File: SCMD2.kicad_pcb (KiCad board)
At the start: 2 copper layers, 86.9 x 68.1 mm, 71 parts, among them IC1 ATMEGA8-P, J1 PWR JACK, J2 ICSP, J3 SKIN_EL, J4 MINIUSB, Q1 2N3904, SW1 SW_GENERIC, SW2 SW_PUSH, U1 OP177, U2 OP177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

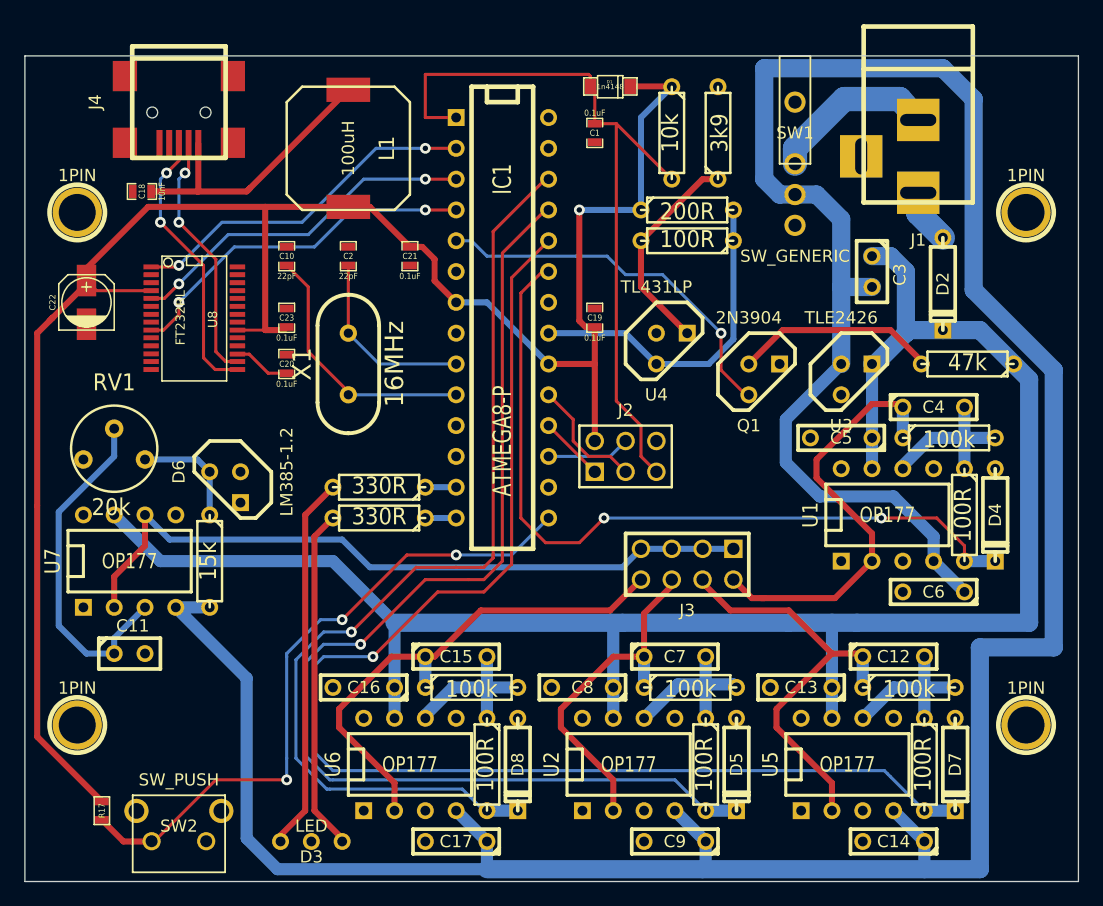
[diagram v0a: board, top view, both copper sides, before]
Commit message: Add filling zone and connect GND.
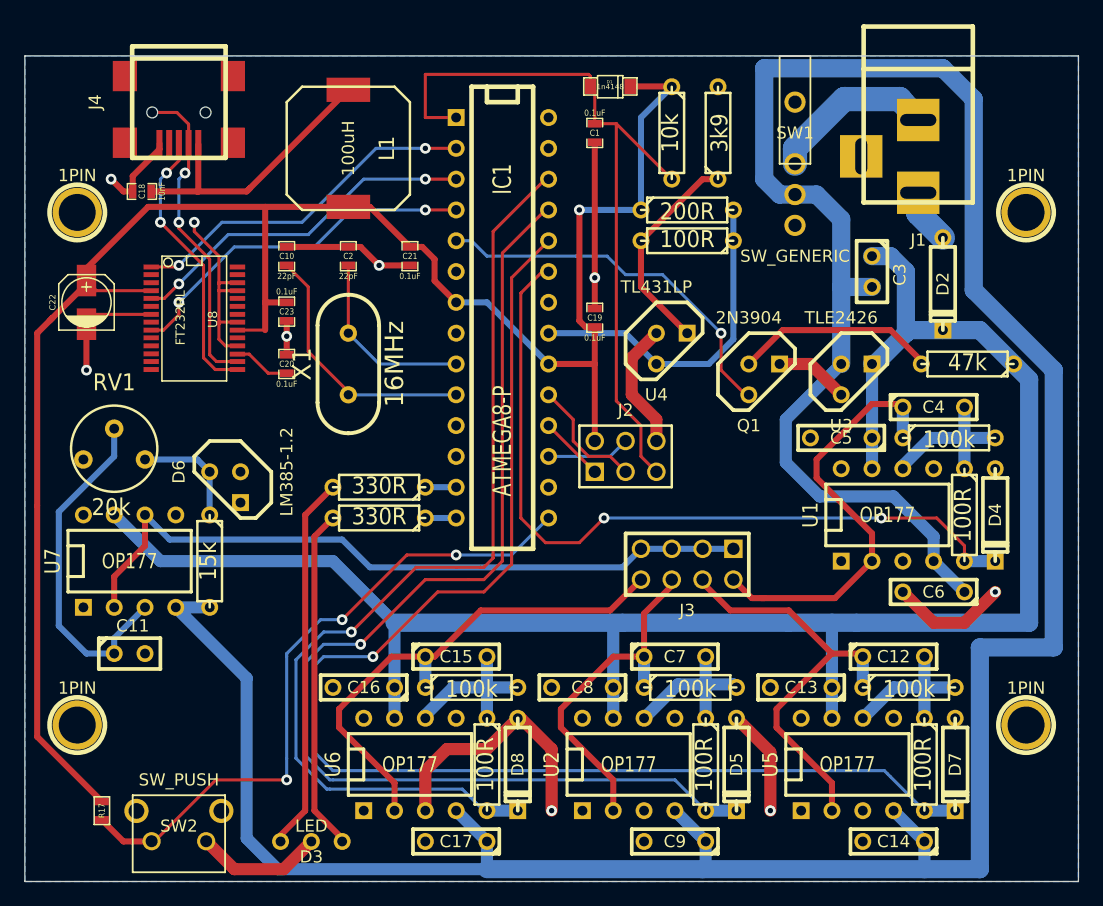
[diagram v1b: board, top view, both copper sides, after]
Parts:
- moved C23 0.51 mm to (49.5, 51.6), turned to 270 degrees
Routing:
- net GND: track 0.00 -> 128.3 mm, vias 0 -> 9
- net N-0000042: track 20.8 -> 26.3 mm
- net +5V: track 159.3 -> 158.5 mm
- added copper zone on B.Cu, net GND

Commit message: Add board info.
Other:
- board text added: "CeDEx Labs, 2014"
- board text added: "SCMD v.0.1"
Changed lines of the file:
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@@
     (area 27.889999 27.614879 114.858001 98.602001)
     (thickness 1.6)
-    (drawings 5)
+    (drawings 7)
     (tracks 477)
     (zones 0)
@@
   )
   (setup
-    (last_trace_width 1)
+    (last_trace_width 0.254)
     (user_trace_width 0.5)
     (user_trace_width 1)
@@
     (visible_elements 7FFFFFFF)
     (pcbplotparams
-      (layerselection 3178497)
+      (layerselection 279609345)
       (usegerberextensions true)
       (excludeedgelayer true)
@@
       (outputformat 1)
       (mirror false)
-      (drillshape 1)
+      (drillshape 0)
       (scaleselection 1)
-      (outputdirectory ""))
+      (outputdirectory gerber/))
   )
   (net 0 "")
@@
     )
   )
+  (gr_text "CeDEx Labs, 2014" (at 66.548 74.676) (layer F.SilkS)
+    (effects (font (size 1.5 1.5) (thickness 0.3)))
+  )
+  (gr_text "SCMD v.0.1" (at 62.738 77.216) (layer F.SilkS)
+    (effects (font (size 1.5 1.5) (thickness 0.3)))
+  )
   (target plus (at 41.91 38.1) (size 0.005) (width 0.1) (layer Edge.Cuts))

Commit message: Fix mini-usb mod and improve ground filling connectivity.
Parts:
- J4: footprint USB_MINI_B -> USB_MINI_B_fixed
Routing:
- net GND: track 128.3 -> 143.9 mm, vias 9 -> 8
- net N-0000042: track 26.3 -> 21.3 mm
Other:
- board text removed: "SCMD v.0.1"
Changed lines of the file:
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@@
 (kicad_pcb (version 3) (host pcbnew "(2013-07-07 BZR 4022)-stable")
   (general
-    (links 155)
+    (links 154)
     (no_connects 0)
     (area 27.889999 27.614879 114.858001 98.602001)
     (thickness 1.6)
-    (drawings 7)
-    (tracks 477)
+    (drawings 6)
+    (tracks 475)
     (zones 0)
     (modules 71)
@@
     (15 F.Cu signal)
     (0 B.Cu signal)
+    (16 B.Adhes user)
     (17 F.Adhes user)
+    (18 B.Paste user)
     (19 F.Paste user)
+    (20 B.SilkS user)
     (21 F.SilkS user)
+    (22 B.Mask user)
     (23 F.Mask user)
     (28 Edge.Cuts user)
   )
   (setup
-    (last_trace_width 0.254)
+    (last_trace_width 1)
     (user_trace_width 0.5)
     (user_trace_width 1)
@@
     (visible_elements 7FFFFFFF)
     (pcbplotparams
-      (layerselection 279609345)
+      (layerselection 285179905)
       (usegerberextensions true)
       (excludeedgelayer true)
@@
       (drillshape 0)
       (scaleselection 1)
-      (outputdirectory gerber/))
+      (outputdirectory D:/xmega128/SCMD2/design/))
   )
   (net 0 "")
@@
     (add_net VEE)
   )
-  (module USB_MINI_B (layer F.Cu)
-    (at 40.64 34.29 270)
-    (descr "USB Mini-B 5-pin SMD connector")
-    (tags "USB, Mini-B, connector")
-    (fp_text reference J4 (at 0 6.90118 270) (layer F.SilkS)
-      (effects (font (size 1.016 1.016) (thickness 0.2032)))
-    )
-    (fp_text value MINIUSB (at 0 -7.0993 270) (layer F.SilkS) hide
-      (effects (font (size 1.016 1.016) (thickness 0.2032)))
-    )
-    (fp_line (start -3.59918 -3.85064) (end -3.59918 3.85064) (layer F.SilkS) (width 0.381))
-    (fp_line (start -4.59994 -3.85064) (end -4.59994 3.85064) (layer F.SilkS) (width 0.381))
-    (fp_line (start -4.59994 3.85064) (end 4.59994 3.85064) (layer F.SilkS) (width 0.381))
-    (fp_line (start 4.59994 3.85064) (end 4.59994 -3.85064) (layer F.SilkS) (width 0.381))
-    (fp_line (start 4.59994 -3.85064) (end -4.59994 -3.85064) (layer F.SilkS) (width 0.381))
-    (pad 1 smd rect (at 3.44932 -1.6002 270) (size 2.30124 0.50038)
-      (layers F.Cu F.Paste F.Mask)
-      (net 29 N-0000041)
-    )
-    (pad 2 smd rect (at 3.44932 -0.8001 270) (size 2.30124 0.50038)
-      (layers F.Cu F.Paste F.Mask)
-      (net 30 N-0000042)
-    )
-    (pad 3 smd rect (at 3.44932 0 270) (size 2.30124 0.50038)
-      (layers F.Cu F.Paste F.Mask)
-      (net 31 N-0000043)
-    )
-    (pad 4 smd rect (at 3.44932 0.8001 270) (size 2.30124 0.50038)
-      (layers F.Cu F.Paste F.Mask)
-    )
-    (pad 5 smd rect (at 3.44932 1.6002 270) (size 2.30124 0.50038)
-      (layers F.Cu F.Paste F.Mask)
-      (net 23 GND)
-    )
-    (pad 6 smd rect (at 3.35026 -4.45008 270) (size 2.49936 1.99898)
-      (layers F.Cu F.Paste F.Mask)
-    )
-    (pad 7 smd rect (at -2.14884 -4.45008 270) (size 2.49936 1.99898)
-      (layers F.Cu F.Paste F.Mask)
-    )
-    (pad 8 smd rect (at 3.35026 4.45008 270) (size 2.49936 1.99898)
-      (layers F.Cu F.Paste F.Mask)
-    )
-    (pad 9 smd rect (at -2.14884 4.45008 270) (size 2.49936 1.99898)
-      (layers F.Cu F.Paste F.Mask)
-    )
-    (pad "" np_thru_hole circle (at 0.8509 -2.19964 270) (size 0.89916 0.89916) (drill 0.89916)
-      (layers *.Cu *.Mask F.SilkS)
-    )
-    (pad 2 np_thru_hole circle (at 0.8509 2.19964 270) (size 0.89916 0.89916) (drill 0.89916)
-      (layers *.Cu *.Mask F.SilkS)
-      (net 30 N-0000042)
-    )
-  )
   (module TO92 (layer F.Cu)
     (at 81.28 54.61)
@@
     )
   )
-  (gr_text "CeDEx Labs, 2014" (at 66.548 74.676) (layer F.SilkS)
-    (effects (font (size 1.5 1.5) (thickness 0.3)))
+  (module USB_MINI_B_fixed (layer F.Cu)
+    (at 40.64 34.29 270)
+    (descr "USB Mini-B 5-pin SMD connector")
+    (tags "USB, Mini-B, connector")
+    (fp_text reference J4 (at 0 6.90118 270) (layer F.SilkS)
+      (effects (font (size 1.016 1.016) (thickness 0.2032)))
+    )
+    (fp_text value MINIUSB (at 0 -7.0993 270) (layer F.SilkS) hide
+      (effects (font (size 1.016 1.016) (thickness 0.2032)))
+    )
+    (fp_line (start -3.59918 -3.85064) (end -3.59918 3.85064) (layer F.SilkS) (width 0.381))
+    (fp_line (start -4.59994 -3.85064) (end -4.59994 3.85064) (layer F.SilkS) (width 0.381))
+    (fp_line (start -4.59994 3.85064) (end 4.59994 3.85064) (layer F.SilkS) (width 0.381))
+    (fp_line (start 4.59994 3.85064) (end 4.59994 -3.85064) (layer F.SilkS) (width 0.381))
+    (fp_line (start 4.59994 -3.85064) (end -4.59994 -3.85064) (layer F.SilkS) (width 0.381))
+    (pad 1 smd rect (at 3.44932 -1.6002 270) (size 2.30124 0.50038)
+      (layers F.Cu F.Paste F.Mask)
+      (net 29 N-0000041)
+    )
+    (pad 2 smd rect (at 3.44932 -0.8001 270) (size 2.30124 0.50038)
+      (layers F.Cu F.Paste F.Mask)
+      (net 30 N-0000042)
+    )
+    (pad 3 smd rect (at 3.44932 0 270) (size 2.30124 0.50038)
+      (layers F.Cu F.Paste F.Mask)
+      (net 31 N-0000043)
+    )
+    (pad 4 smd rect (at 3.44932 0.8001 270) (size 2.30124 0.50038)
+      (layers F.Cu F.Paste F.Mask)
+    )
+    (pad 5 smd rect (at 3.44932 1.6002 270) (size 2.30124 0.50038)
+      (layers F.Cu F.Paste F.Mask)
+      (net 23 GND)
+    )
+    (pad 6 smd rect (at 3.35026 -4.45008 270) (size 2.49936 1.99898)
+      (layers F.Cu F.Paste F.Mask)
+    )
+    (pad 7 smd rect (at -2.14884 -4.45008 270) (size 2.49936 1.99898)
+      (layers F.Cu F.Paste F.Mask)
+    )
+    (pad 8 smd rect (at 3.35026 4.45008 270) (size 2.49936 1.99898)
+      (layers F.Cu F.Paste F.Mask)
+    )
+    (pad 9 smd rect (at -2.14884 4.45008 270) (size 2.49936 1.99898)
+      (layers F.Cu F.Paste F.Mask)
+    )
+    (pad "" np_thru_hole circle (at 0.8509 -2.19964 270) (size 0.89916 0.89916) (drill 0.89916)
+      (layers *.Cu *.Mask F.SilkS)
+    )
+    (pad "" np_thru_hole circle (at 0.8509 2.19964 270) (size 0.89916 0.89916) (drill 0.89916)
+      (layers *.Cu *.Mask F.SilkS)
+    )
   )
-  (gr_text "SCMD v.0.1" (at 62.738 77.216) (layer F.SilkS)
+  (gr_text "CeDEx Labs, 2014" (at 66.548 74.676) (layer F.SilkS)
     (effects (font (size 1.5 1.5) (thickness 0.3)))
   )
@@
   (segment (start 51.308 54.864) (end 51.308 49.53) (width 0.254) (layer F.Cu) (net 22))
   (segment (start 54.61 58.166) (end 51.308 54.864) (width 0.254) (layer F.Cu) (net 22))
+  (segment (start 100.33 74.676) (end 102.87 77.216) (width 1) (layer F.Cu) (net 23) (status 400000))
+  (segment (start 110.744 67.31) (end 107.95 64.516) (width 1) (layer F.Cu) (net 23) (status 800000))
+  (segment (start 110.744 67.564) (end 110.744 67.31) (width 1) (layer F.Cu) (net 23))
+  (segment (start 110.744 77.216) (end 110.744 67.564) (width 1) (layer F.Cu) (net 23))
+  (segment (start 102.87 77.216) (end 110.744 77.216) (width 1) (layer F.Cu) (net 23))
   (segment (start 80.01 62.23) (end 80.01 60.452) (width 1) (layer F.Cu) (net 23))
   (segment (start 77.978 55.372) (end 80.01 53.34) (width 1) (layer F.Cu) (net 23))
   (segment (start 77.978 58.42) (end 77.978 55.372) (width 1) (layer F.Cu) (net 23))
   (segment (start 80.01 60.452) (end 77.978 58.42) (width 1) (layer F.Cu) (net 23))
-  (segment (start 100.33 74.676) (end 102.87 77.216) (width 1) (layer F.Cu) (net 23))
-  (via (at 107.95 74.676) (size 0.889) (layers F.Cu B.Cu) (net 23))
-  (segment (start 105.41 77.216) (end 107.95 74.676) (width 1) (layer F.Cu) (net 23))
-  (segment (start 102.87 77.216) (end 105.41 77.216) (width 1) (layer F.Cu) (net 23))
   (segment (start 60.96 92.71) (end 60.96 89.408) (width 1) (layer F.Cu) (net 23))
   (segment (start 66.04 87.63) (end 68.58 85.09) (width 1) (layer F.Cu) (net 23))
@@
   (segment (start 46.482 41.402) (end 54.61 33.274) (width 0.5) (layer F.Cu) (net 29))
   (segment (start 42.164 37.81552) (end 42.2402 37.73932) (width 0.254) (layer F.Cu) (net 29))
-  (segment (start 38.44036 35.1409) (end 40.4749 35.1409) (width 0.254) (layer F.Cu) (net 30))
-  (segment (start 41.4401 36.1061) (end 41.4401 37.73932) (width 0.254) (layer F.Cu) (net 30))
-  (segment (start 40.4749 35.1409) (end 41.4401 36.1061) (width 0.254) (layer F.Cu) (net 30))
   (segment (start 40.64 44.196) (end 40.64 44.704) (width 0.254) (layer F.Cu) (net 30))
   (via (at 40.64 44.196) (size 0.889) (layers F.Cu B.Cu) (net 30))

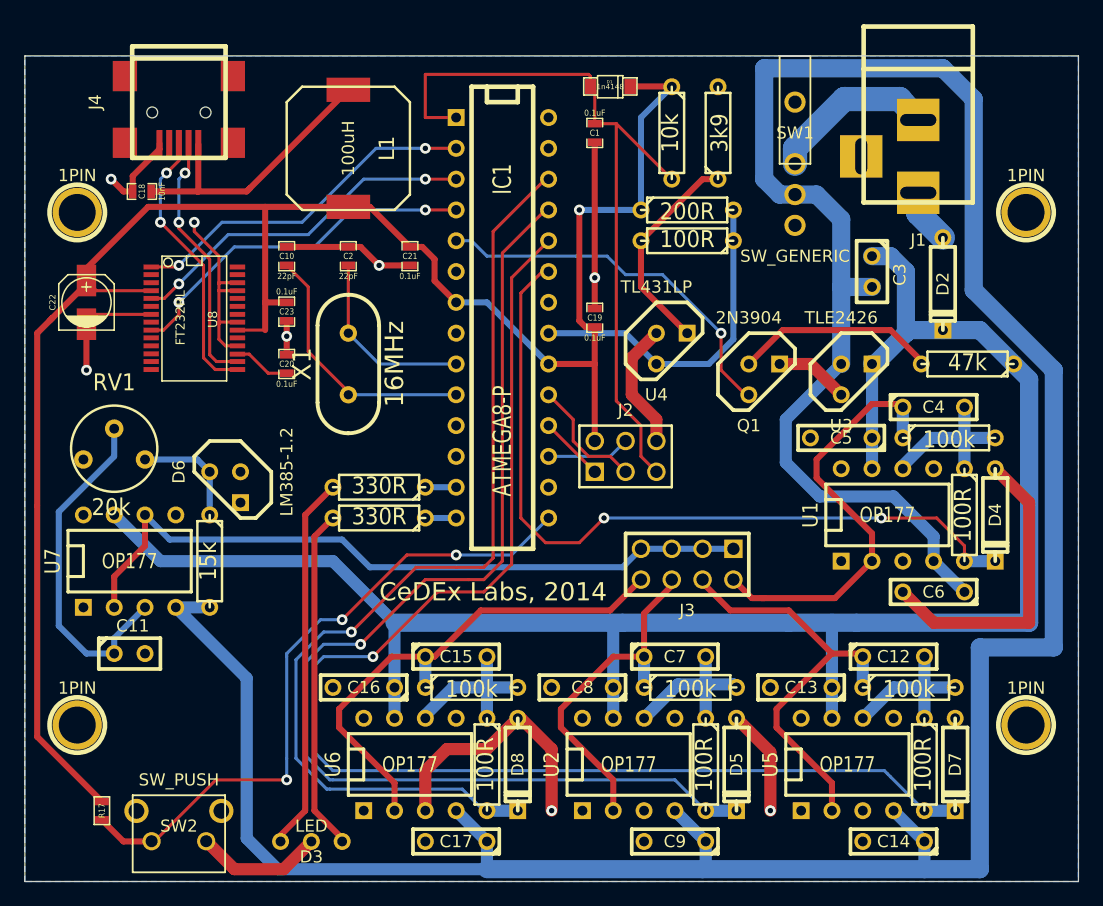
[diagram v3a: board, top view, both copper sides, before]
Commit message: Refactor PCB and release SCMD2 V.0.1.2
* Fix L1 footprint,
* Refactor tracks to avoid their accidential damage,
* Replace TO92 footprints to match case type,
* Use SM0603 for R1,
* Add pin labels for J2 and J3,
* Add D3 LED labels,
* Add board version label.
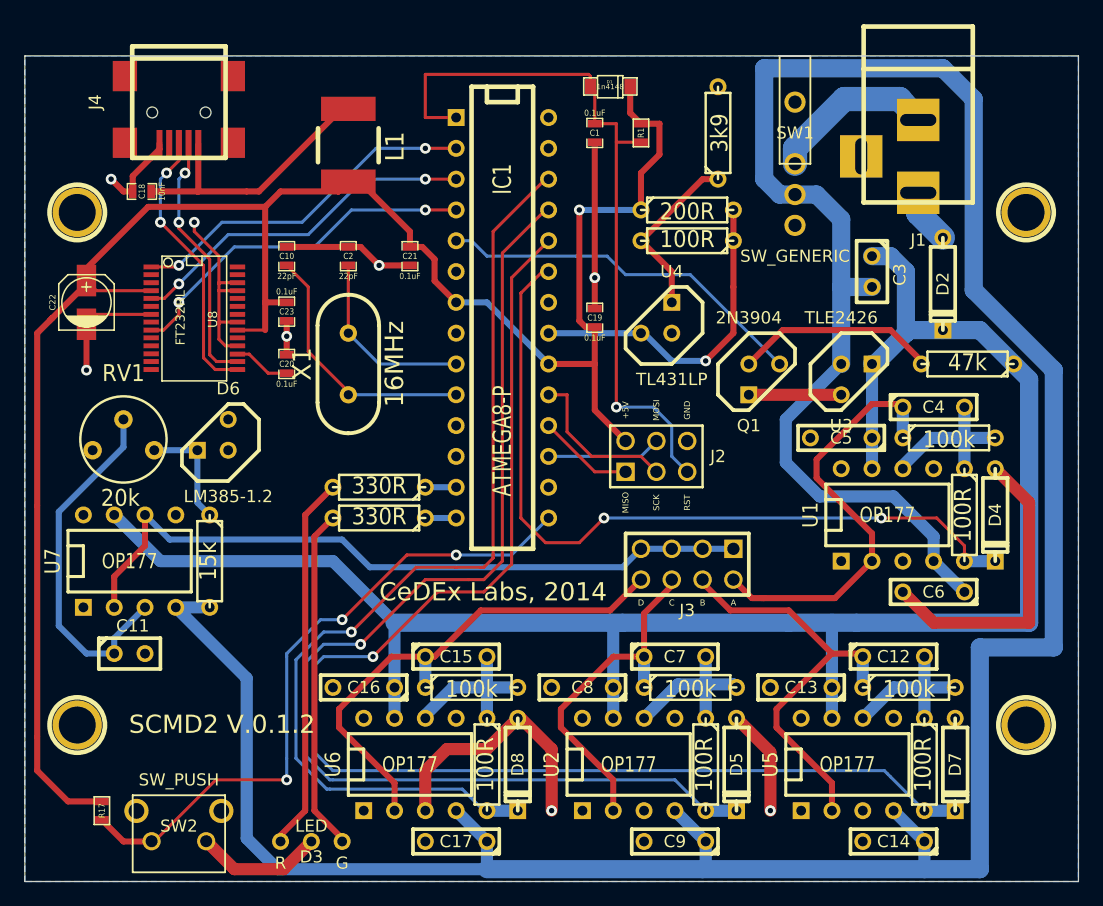
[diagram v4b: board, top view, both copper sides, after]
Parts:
- D6: footprint TO92-123 -> TO92
- J2: footprint pin_array_3x2 -> pin_array_3x2_ICSP
- J3: footprint pin_array_4x2 -> pin_array_4x2_SKIN_EL
- L1: footprint self_cms_we-tpc_XL -> Neosid_Inductor_SM-NE56_SMD2220_RevA_21Apr2012
- Q1, U4: footprint TO92 -> TO92-INVERT
- R1: footprint R3 -> SM0603
- moved D6 4.44 mm to (43.4, 61.7), turned to 180 degrees
- moved U4 2.84 mm to (80.0, 52.1), turned to 180 degrees
- moved J2 2.54 mm to (80.0, 63.5)
- moved R1 2.54 mm to (78.7, 36.8)
- moved RV1 1.08 mm to (36.1, 61.7)
- moved L1 0.25 mm to (54.6, 37.8)
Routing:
- net GND: track 143.9 -> 134.8 mm
- net +5V: track 158.5 -> 164.6 mm
- net /SCK: track 10.0 -> 13.3 mm
- net N-0000044: track 17.7 -> 14.6 mm
- net /MOSI: track 6.88 -> 9.42 mm
- net /MISO: track 5.64 -> 8.18 mm
- net /RESET: track 62.1 -> 60.5 mm, vias 0 -> 1
- net N-0000062: track 28.5 -> 29.6 mm
- net N-0000041: track 24.1 -> 23.2 mm
- net /AREF: track 27.8 -> 27.3 mm, vias 0 -> 1
- net /A-PWR: vias 1 -> 0
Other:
- board text added: "G"
- board text added: "R"
- board text added: "SCMD2 V.0.1.2"
